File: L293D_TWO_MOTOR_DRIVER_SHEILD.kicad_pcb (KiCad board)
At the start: 2 copper layers, 68.7 x 53.4 mm, 24 parts, among them J1 4.5VDC to 36VDC, J2 Servo02, J3 Servo01, J4 Conn_01x04_Male, J5 Conn_01x04_Male, J6 S, J7 Potent. I/P, J8 Conn_01x04_Male, SW2 SW_Push, U1 L293D

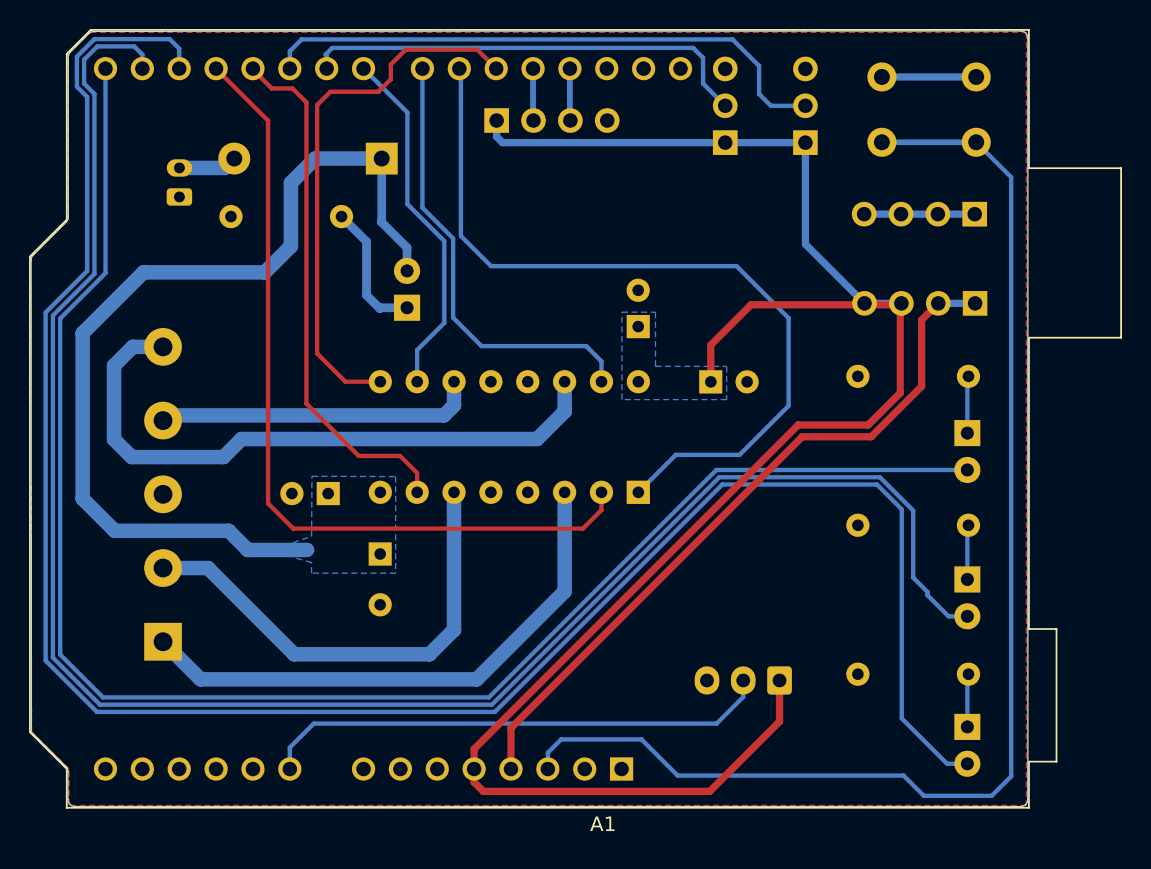
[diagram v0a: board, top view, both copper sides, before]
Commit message: updated LED placement for digital IOs 0,1,2
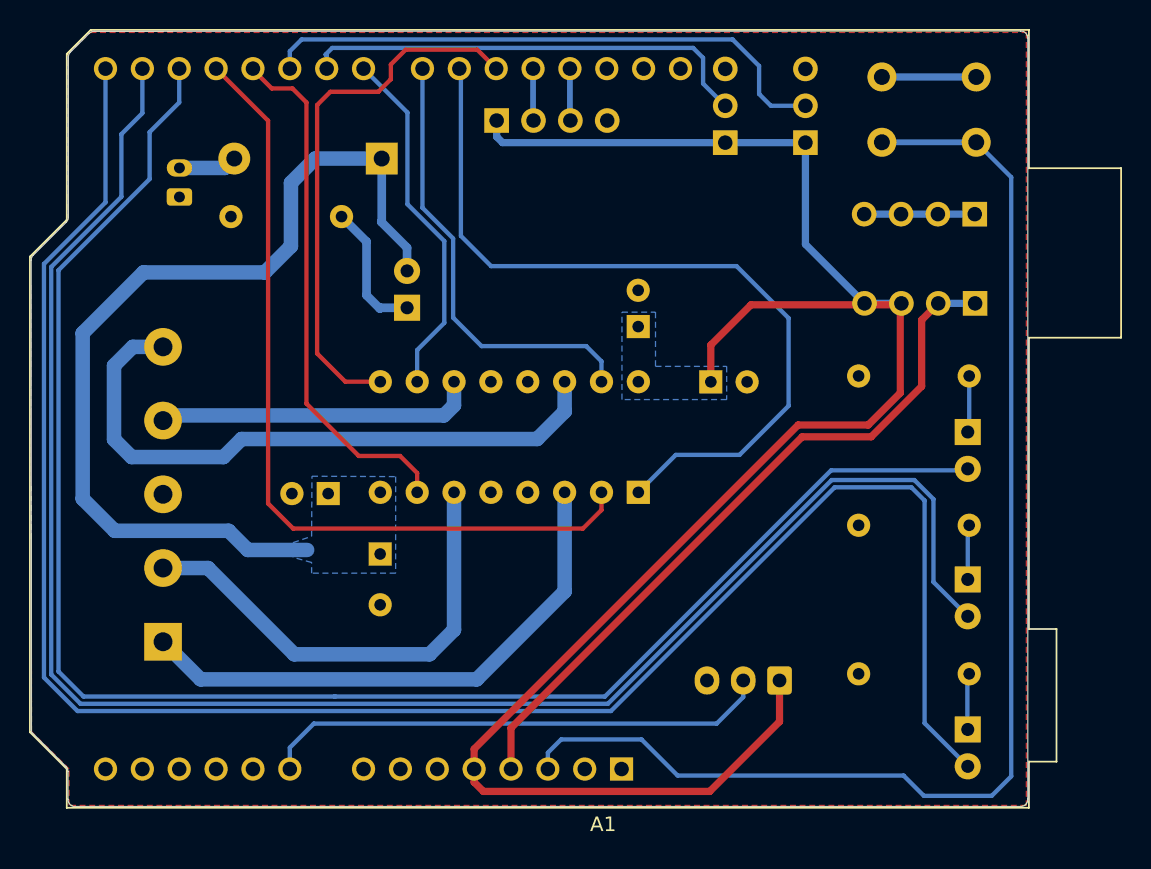
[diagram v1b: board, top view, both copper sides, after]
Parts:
- moved R4 20.5 mm to (170.6, 100.5)
- moved R2 20.5 mm to (170.6, 121.0)
- moved D3 20.4 mm to (170.5, 124.8)
- moved D5 20.3 mm to (170.5, 104.3)
- moved R3 0.05 mm to (170.6, 110.8)
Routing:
- net Net-(A1-D2): track 140.2 -> 114.9 mm
- net Net-(A1-D0/RX): track 111.9 -> 131.7 mm
- net Net-(A1-D1/TX): track 125.9 -> 122.0 mm
